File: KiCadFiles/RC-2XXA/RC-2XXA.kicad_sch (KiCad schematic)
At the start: 252 parts, among them J1 Conn_01x01_Pin, J2 Conn_01x04_Pin, J3 Conn_01x04_Pin, J4 Conn_01x07_Socket, J5 Conn_01x07_Socket, SW1 SW_DPST_x2, SW2 SW_DPST_x2, U1 TLV74318PDBVR, U2 PMW3360DM-T2QU, U3 TPD4E05U06DQAR, U4 STM32F072CBTx, U5 XC6206PxxxMR

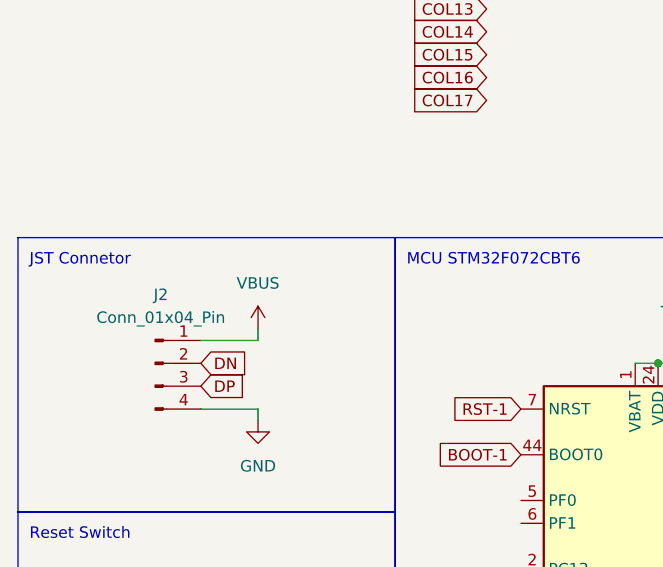
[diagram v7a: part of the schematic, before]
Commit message: Update RC-2XXA project files: Adjust minimum clearance and modify connector properties
- Changed minimum clearance in RC-2XXA.kicad_pro from 0.5 to 0.26.
- Updated the "Value" property of a component in RC-2XXA.kicad_sch from "VBUS" to "+5V".
- Added a new connector symbol with detailed properties including reference, value, footprint, and description.
- Removed the old connector symbol to avoid duplication.
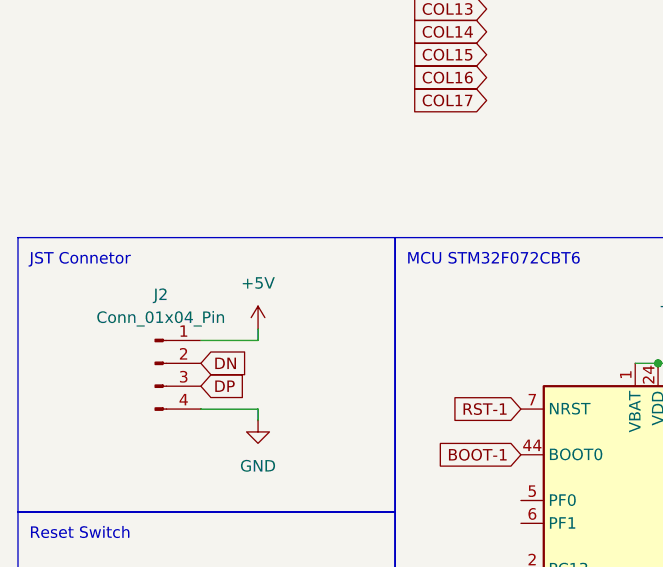
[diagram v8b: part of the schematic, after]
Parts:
- J3: footprint Connector_PinHeader_1.27mm:PinHeader_1x04_P1.27mm_Vertical -> My-Fi Footprints:My-SolderWire-0.5sqmm_1x04_D0.9mm_OD2.1mm; MPN C160404 -> (none)
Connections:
- net +5V: now also J2.1 (Pin_1)
- net VBUS: no longer J2.1 (Pin_1)
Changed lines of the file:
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@@
 			)
 		)
-		(property "Value" "VBUS"
+		(property "Value" "+5V"
 			(at 40.64 308.61 0)
 			(effects
@@
 	)
 	(symbol
+		(lib_id "Connector:Conn_01x04_Pin")
+		(at 233.68 344.17 0)
+		(unit 1)
+		(exclude_from_sim no)
+		(in_bom yes)
+		(on_board yes)
+		(dnp no)
+		(fields_autoplaced yes)
+		(property "Reference" "J3"
+			(at 234.315 336.55 0)
+			(effects
+				(font
+					(size 1.27 1.27)
+				)
+			)
+		)
+		(property "Value" "Conn_01x04_Pin"
+			(at 234.315 339.09 0)
+			(effects
+				(font
+					(size 1.27 1.27)
+				)
+			)
+		)
+		(property "Footprint" "My-Fi Footprints:My-SolderWire-0.5sqmm_1x04_D0.9mm_OD2.1mm"
+			(at 233.68 344.17 0)
+			(effects
+				(font
+					(size 1.27 1.27)
+				)
+				(hide yes)
+			)
+		)
+		(property "Datasheet" "~"
+			(at 233.68 344.17 0)
+			(effects
+				(font
+					(size 1.27 1.27)
+				)
+				(hide yes)
+			)
+		)
+		(property "Description" "Generic connector, single row, 01x04, script generated"
+			(at 233.68 344.17 0)
+			(effects
+				(font
+					(size 1.27 1.27)
+				)
+				(hide yes)
+			)
+		)
+		(pin "2"
+		)
+		(pin "1"
+		)
+		(pin "3"
+		)
+		(pin "4"
+		)
+		(instances
+			(project ""
+				(path "/65196bbe-5350-405f-9fe2-667d33111e14"
+					(reference "J3")
+					(unit 1)
+				)
+			)
+		)
+	)
+	(symbol
 		(lib_id "Device:R_Small")
 		(at 152.4 309.88 90)
@@
 					(unit 1)
 				)
-			)
-		)
-	)
-	(symbol
-		(lib_id "Connector:Conn_01x04_Pin")
-		(at 233.68 344.17 0)
-		(unit 1)
-		(exclude_from_sim no)
-		(in_bom yes)
-		(on_board yes)
-		(dnp no)
-		(fields_autoplaced yes)
-		(property "Reference" "J3"
-			(at 234.315 336.55 0)
-			(effects
-				(font
-					(size 1.27 1.27)
-				)
-			)
-		)
-		(property "Value" "Conn_01x04_Pin"
-			(at 234.315 339.09 0)
-			(effects
-				(font
-					(size 1.27 1.27)
-				)
-			)
-		)
-		(property "Footprint" "Connector_PinHeader_1.27mm:PinHeader_1x04_P1.27mm_Vertical"
-			(at 233.68 344.17 0)
-			(effects
-				(font
-					(size 1.27 1.27)
-				)
-				(hide yes)
-			)
-		)
-		(property "Datasheet" "~"
-			(at 233.68 344.17 0)
-			(effects
-				(font
-					(size 1.27 1.27)
-				)
-				(hide yes)
-			)
-		)
-		(property "Description" "Generic connector, single row, 01x04, script generated"
-			(at 233.68 344.17 0)
-			(effects
-				(font
-					(size 1.27 1.27)
-				)
-				(hide yes)
-			)
-		)
-		(property "MPN" "C160404"
-			(at 233.68 344.17 0)
-			(effects
-				(font
-					(size 1.27 1.27)
-				)
-				(hide yes)
-			)
-		)
-		(pin "3"
-		)
-		(pin "1"
-		)
-		(pin "2"
-		)
-		(pin "4"
-		)
-		(instances
-			(project "RC-2XXA"
-				(path "/65196bbe-5350-405f-9fe2-667d33111e14"
-					(reference "J3")
-					(unit 1)
-				)
